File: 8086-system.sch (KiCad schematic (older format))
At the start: 0 parts

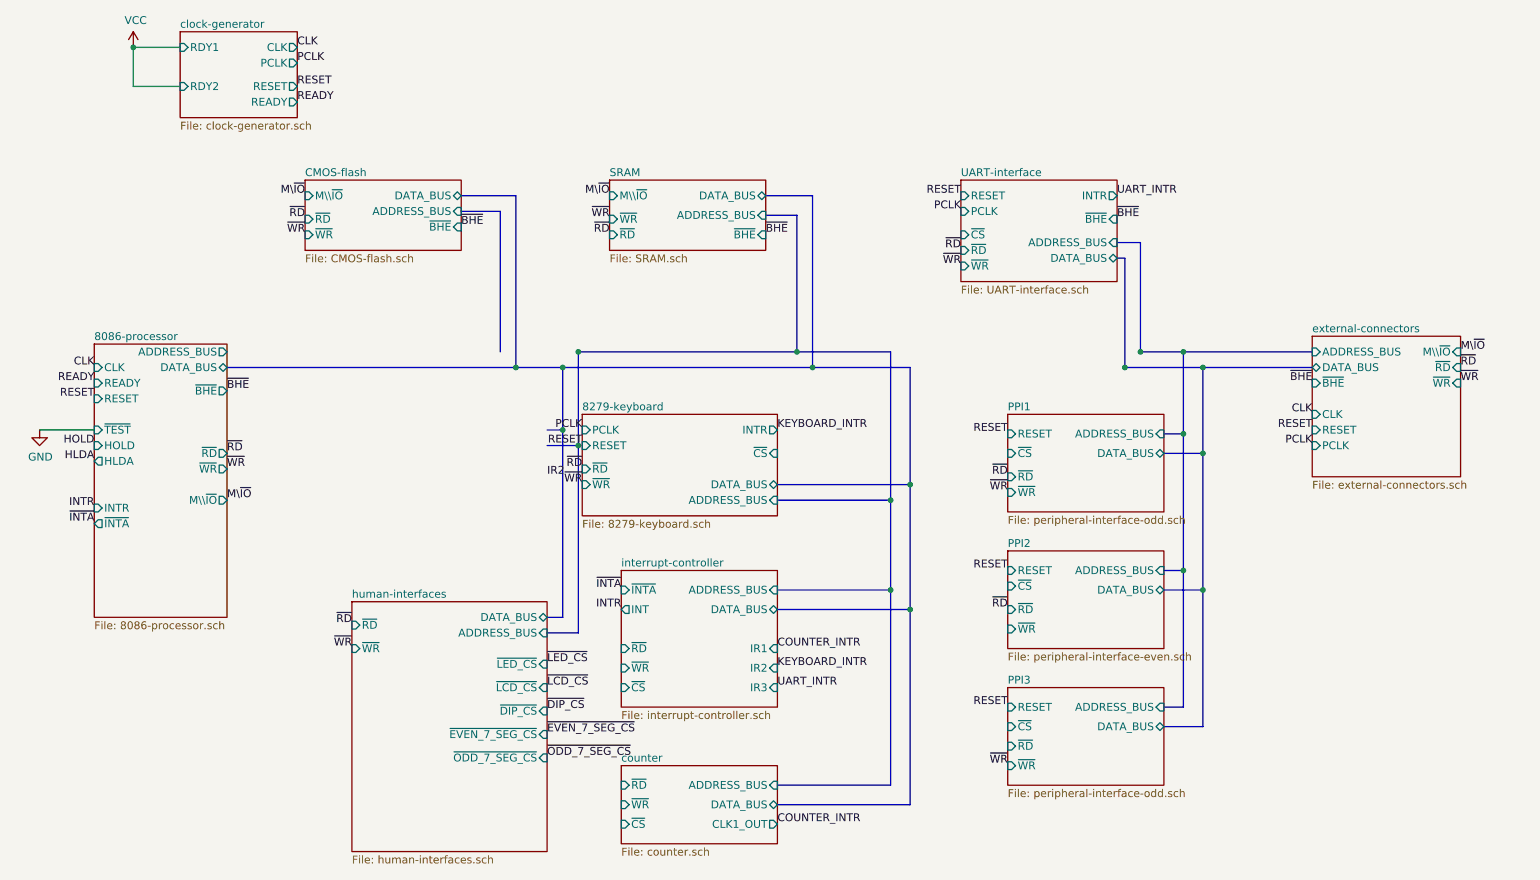
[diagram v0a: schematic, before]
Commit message: Fix wiring in root sheet
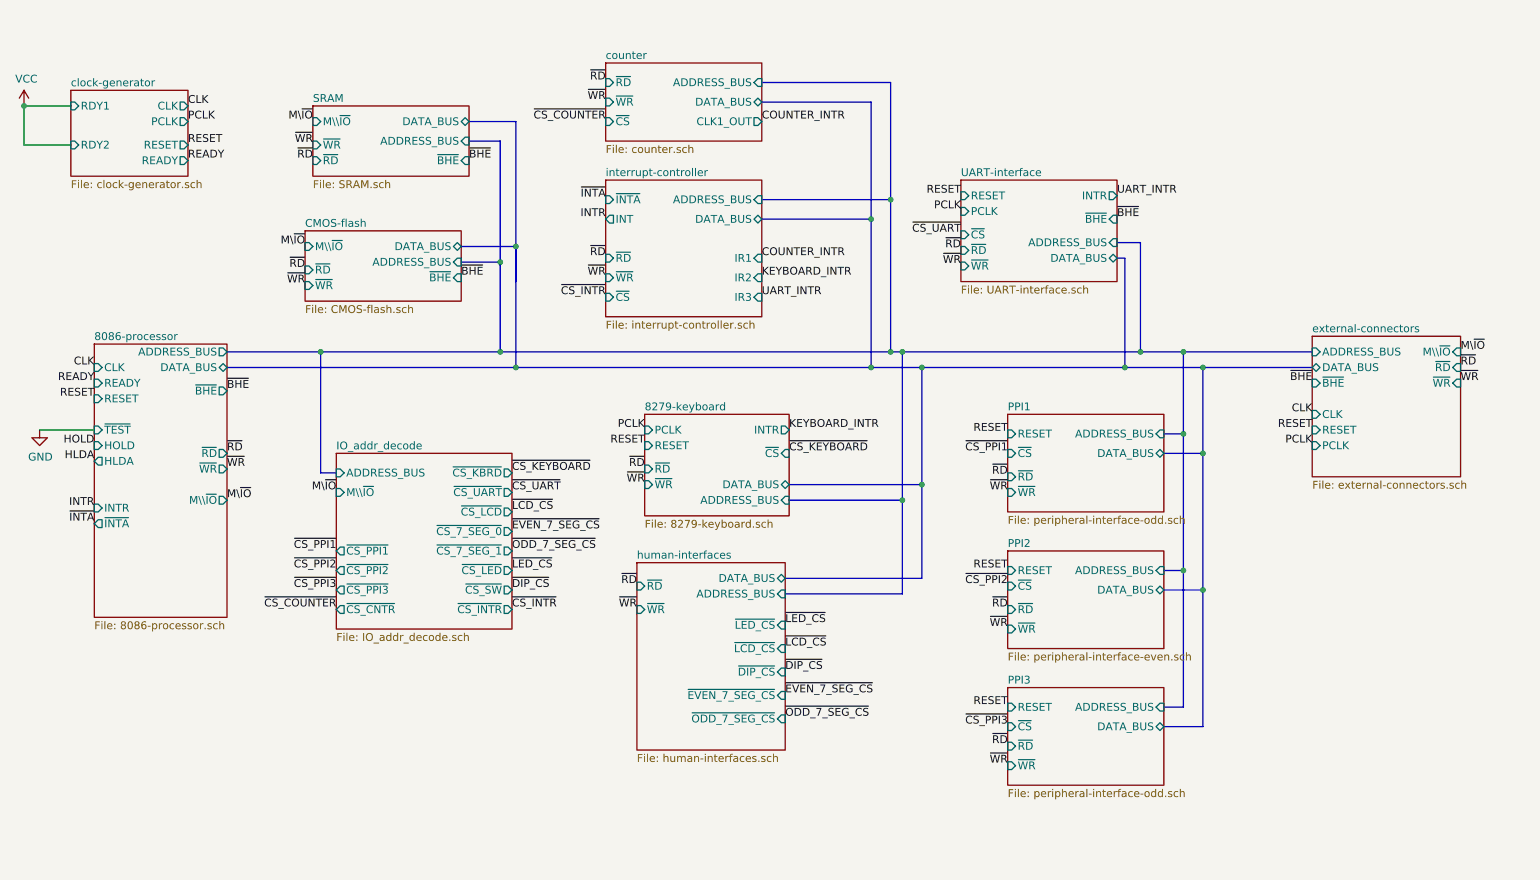
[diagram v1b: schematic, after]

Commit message: Decode BHE for IO addresses
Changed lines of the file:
@@
 F14 "~CS_7_SEG_0" O R 3825 4250 50
 F15 "~CS_7_SEG_1" O R 3825 4375 50
+F16 "~BHE" I L 2700 4125 50
 $EndSheet
 Connection ~ 6325 3100
@@
 Text Label 4675 3700 2    50   ~ 0
 RESET
+Text Label 2700 4125 2    50   ~ 0
+~BHE
 $EndSCHEMATC

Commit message: General edits; removed floating inputs
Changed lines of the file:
@@
 F4 "RESET" O R 1750 1775 50
 F5 "READY" O R 1750 1875 50
-F6 "RDY1" I L 1000 1525 50
-F7 "RDY2" I L 1000 1775 50
 $EndSheet
 Text Label 1750 1525 0    50   ~ 0
@@
 Text Label 1750 1775 0    50   ~ 0
 RESET
-Wire Wire Line
-	1150 3600 800  3600
-$Comp
-L power:GND #PWR0103
-U 1 1 61966AE7
-P 800 3600
-F 0 "#PWR0103" H 800 3350 50  0001 C CNN
-F 1 "GND" H 805 3427 50  0000 C CNN
-F 2 "" H 800 3600 50  0001 C CNN
-F 3 "" H 800 3600 50  0001 C CNN
-	1    800  3600
-	1    0    0    -1
-$EndComp
-Wire Wire Line
-	700  1525 700  1775
-$Comp
-L power:VCC #PWR0104
-U 1 1 61967609
-P 700 1525
-F 0 "#PWR0104" H 700 1375 50  0001 C CNN
-F 1 "VCC" H 715 1698 50  0000 C CNN
-F 2 "" H 700 1525 50  0001 C CNN
-F 3 "" H 700 1525 50  0001 C CNN
-	1    700  1525
-	1    0    0    -1
-$EndComp
-Wire Wire Line
-	1000 1775 700  1775
-Wire Wire Line
-	1000 1525 700  1525
-Connection ~ 700  1525
 Text Label 8950 3600 2    50   ~ 0
 RESET
@@
 F6 "RESET" I L 1150 3400 50
 F7 "READY" I L 1150 3300 50
-F8 "~TEST" I L 1150 3600 50
-F9 "HOLD" I L 1150 3700 50
-F10 "HLDA" O L 1150 3800 50
-F11 "~INTA" O L 1150 4200 50
-F12 "DATA_BUS" B R 2000 3200 50
-F13 "M\\~IO" O R 2000 4050 50
-F14 "~WR" O R 2000 3850 50
-F15 "~RD" O R 2000 3750 50
+F8 "HOLD" I L 1150 3700 50
+F9 "HLDA" O L 1150 3800 50
+F10 "~INTA" O L 1150 4200 50
+F11 "DATA_BUS" B R 2000 3200 50
+F12 "M\\~IO" O R 2000 4050 50
+F13 "~WR" O R 2000 3850 50
+F14 "~RD" O R 2000 3750 50
 $EndSheet
 Text Label 2000 3750 0    50   ~ 0

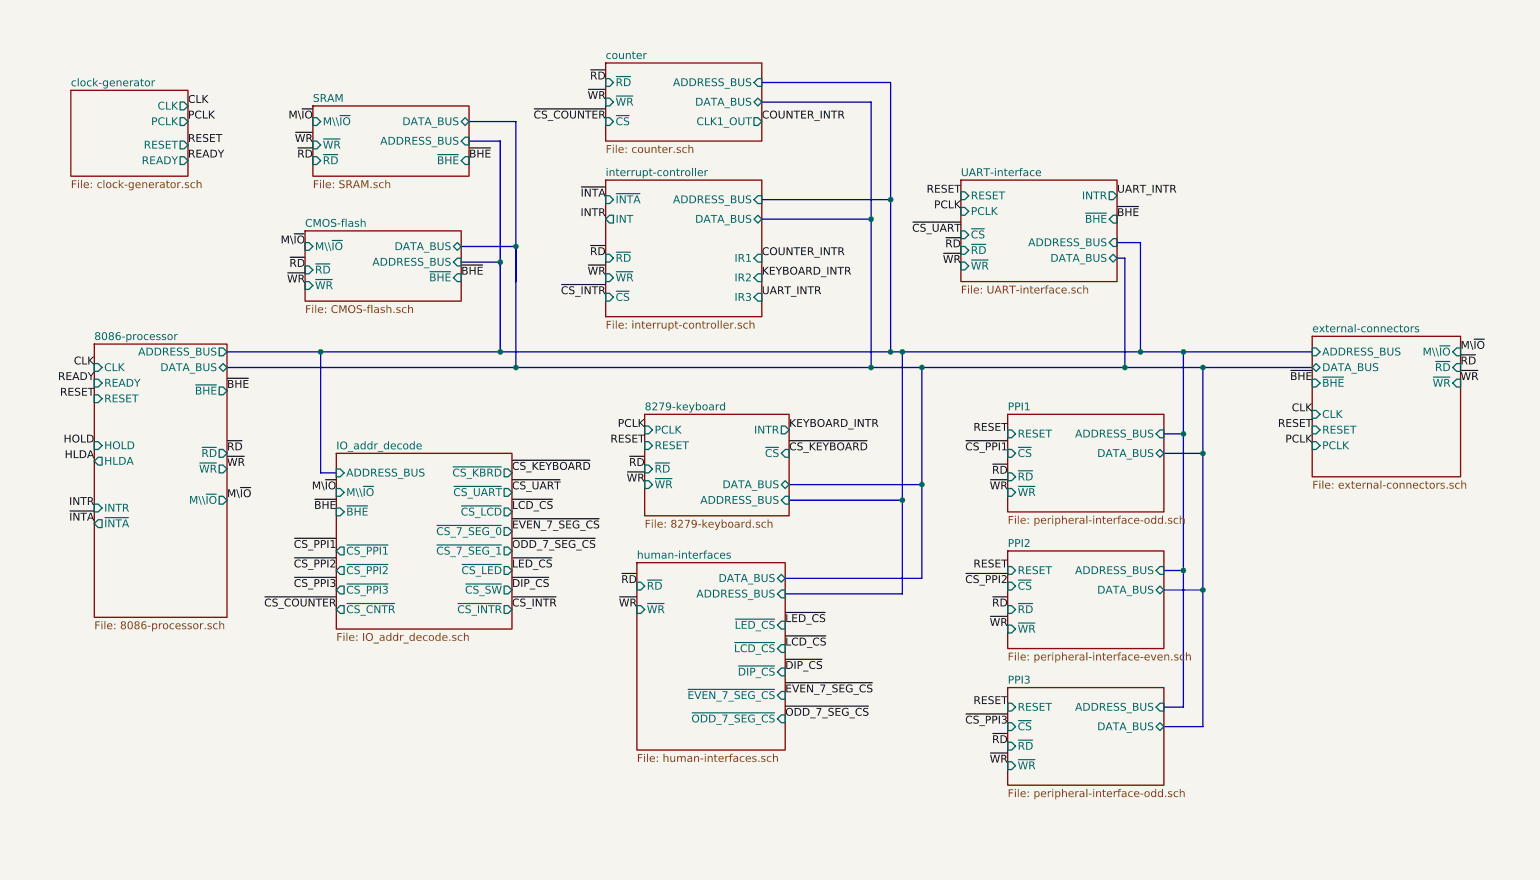
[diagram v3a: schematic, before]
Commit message: Updates to pass ERC
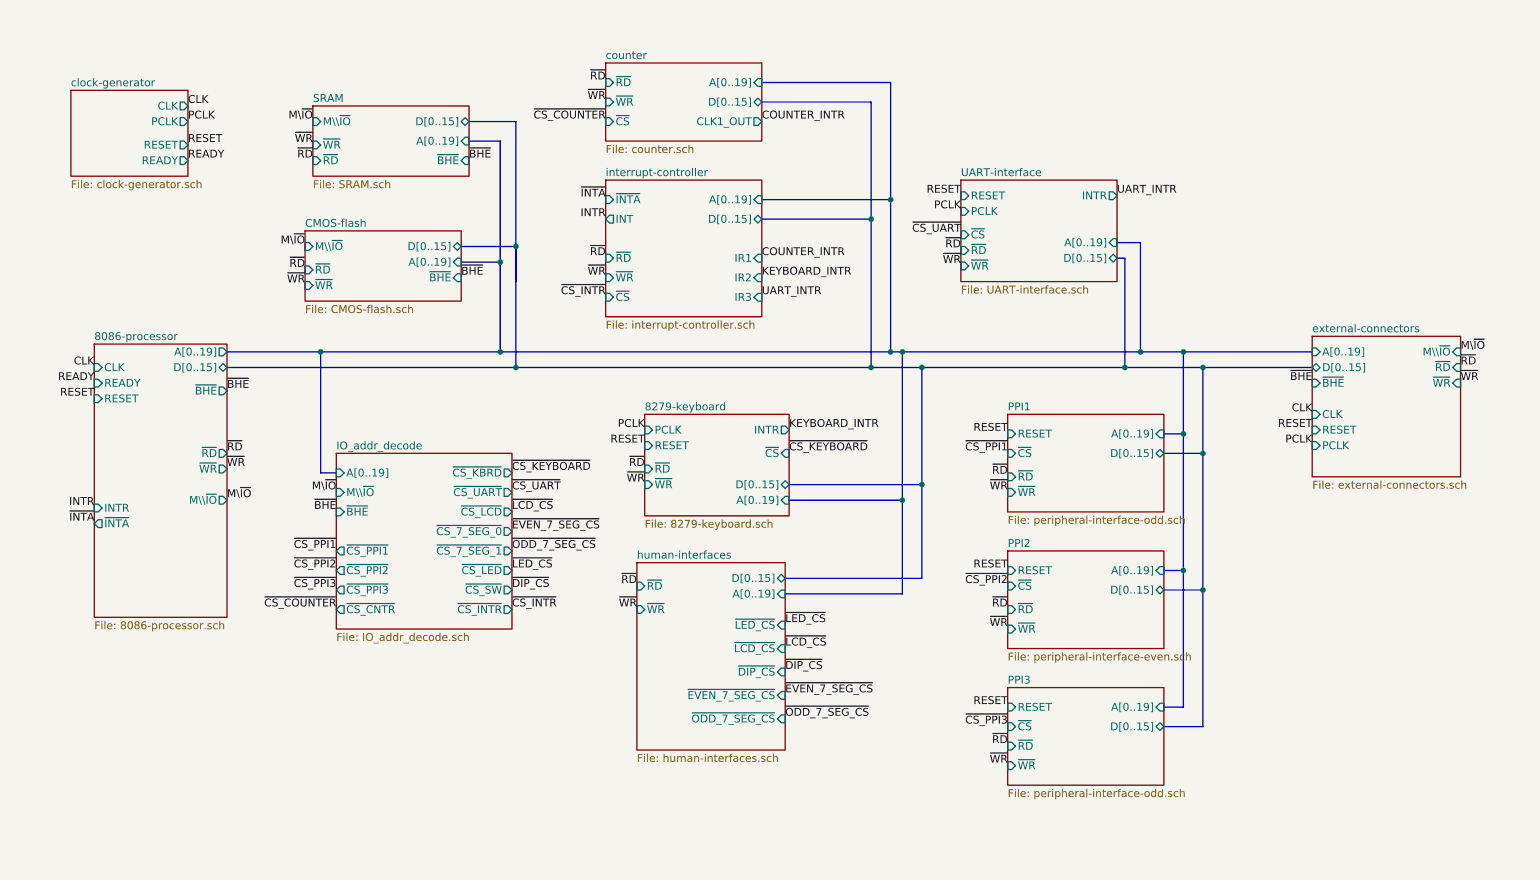
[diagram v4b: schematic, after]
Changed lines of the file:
@@
 F1 "external-connectors.sch" 50
 F2 "~BHE" I L 8950 3300 50
-F3 "DATA_BUS" B L 8950 3200 50
-F4 "ADDRESS_BUS" I L 8950 3100 50
+F3 "D[0..15]" B L 8950 3200 50
+F4 "A[0..19]" I L 8950 3100 50
 F5 "CLK" I L 8950 3500 50
 F6 "PCLK" I L 8950 3700 50
@@
 Text Label 1150 3400 2    50   ~ 0
 RESET
-Text Label 1150 3700 2    50   ~ 0
-HOLD
-Text Label 1150 3800 2    50   ~ 0
-HLDA
 Text Label 1150 4100 2    50   ~ 0
 INTR
@@
 F2 "INTR" O R 7700 2100 50
 F3 "PCLK" I L 6700 2200 50
-F4 "DATA_BUS" B R 7700 2500 50
+F4 "D[0..15]" B R 7700 2500 50
 F5 "RESET" I L 6700 2100 50
-F6 "ADDRESS_BUS" I R 7700 2400 50
-F7 "~BHE" I R 7700 2250 50
-F8 "~RD" I L 6700 2450 50
-F9 "~WR" I L 6700 2550 50
-F10 "~CS" I L 6700 2350 50
-$EndSheet
-Text Label 7700 2250 0    50   ~ 0
-~BHE
+F6 "A[0..19]" I R 7700 2400 50
+F7 "~RD" I L 6700 2450 50
+F8 "~WR" I L 6700 2550 50
+F9 "~CS" I L 6700 2350 50
+$EndSheet
 Text Label 7700 2100 0    50   ~ 0
 UART_INTR
@@
 F0 "SRAM" 50
 F1 "SRAM.sch" 50
-F2 "ADDRESS_BUS" I R 3550 1750 50
+F2 "A[0..19]" I R 3550 1750 50
 F3 "M\\~IO" I L 2550 1625 50
 F4 "~BHE" I R 3550 1875 50
 F5 "~RD" I L 2550 1875 50
 F6 "~WR" I L 2550 1775 50
-F7 "DATA_BUS" B R 3550 1625 50
+F7 "D[0..15]" B R 3550 1625 50
 $EndSheet
 Wire Bus Line
@@
 F4 "~RD" I L 7000 5625 50
 F5 "~WR" I L 7000 5750 50
-F6 "DATA_BUS" B R 8000 5500 50
-F7 "ADDRESS_BUS" I R 8000 5375 50
+F6 "D[0..15]" B R 8000 5500 50
+F7 "A[0..19]" I R 8000 5375 50
 $EndSheet
 $Sheet
@@
 F4 "~RD" I L 7000 3900 50
 F5 "~WR" I L 7000 4000 50
-F6 "DATA_BUS" B R 8000 3750 50
-F7 "ADDRESS_BUS" I R 8000 3625 50
+F6 "D[0..15]" B R 8000 3750 50
+F7 "A[0..19]" I R 8000 3625 50
 $EndSheet
 $Sheet
@@
 F4 "~RD" I L 7000 4750 50
 F5 "~WR" I L 7000 4875 50
-F6 "DATA_BUS" B R 8000 4625 50
-F7 "ADDRESS_BUS" I R 8000 4500 50
+F6 "D[0..15]" B R 8000 4625 50
+F7 "A[0..19]" I R 8000 4500 50
 $EndSheet
 $Sheet
@@
 F3 "IR2" I R 5425 2625 50
 F4 "IR3" I R 5425 2750 50
-F5 "DATA_BUS" B R 5425 2250 50
+F5 "D[0..15]" B R 5425 2250 50
 F6 "~CS" I L 4425 2750 50
 F7 "~WR" I L 4425 2625 50
@@
 F9 "INT" O L 4425 2250 50
 F10 "~INTA" I L 4425 2125 50
-F11 "ADDRESS_BUS" I R 5425 2125 50
+F11 "A[0..19]" I R 5425 2125 50
 $EndSheet
 Text Label 5600 3600 0    50   ~ 0
@@
 F3 "INTR" O R 5600 3600 50
 F4 "RESET" I L 4675 3700 50
-F5 "DATA_BUS" B R 5600 3950 50
-F6 "ADDRESS_BUS" I R 5600 4050 50
+F5 "D[0..15]" B R 5600 3950 50
+F6 "A[0..19]" I R 5600 4050 50
 F7 "~RD" I L 4675 3850 50
 F8 "~WR" I L 4675 3950 50
@@
 F0 "counter" 50
 F1 "counter.sch" 50
-F2 "DATA_BUS" B R 5425 1500 50
+F2 "D[0..15]" B R 5425 1500 50
 F3 "~RD" I L 4425 1375 50
 F4 "~WR" I L 4425 1500 50
-F5 "ADDRESS_BUS" I R 5425 1375 50
+F5 "A[0..19]" I R 5425 1375 50
 F6 "~CS" I L 4425 1625 50
 F7 "CLK1_OUT" O R 5425 1625 50
@@
 F1 "8086-processor.sch" 50
 F2 "CLK" I L 1150 3200 50
-F3 "ADDRESS_BUS" O R 2000 3100 50
+F3 "A[0..19]" O R 2000 3100 50
 F4 "~BHE" O R 2000 3350 50
 F5 "INTR" I L 1150 4100 50
 F6 "RESET" I L 1150 3400 50
 F7 "READY" I L 1150 3300 50
-F8 "HOLD" I L 1150 3700 50
-F9 "HLDA" O L 1150 3800 50
-F10 "~INTA" O L 1150 4200 50
-F11 "DATA_BUS" B R 2000 3200 50
-F12 "M\\~IO" O R 2000 4050 50
-F13 "~WR" O R 2000 3850 50
-F14 "~RD" O R 2000 3750 50
+F8 "~INTA" O L 1150 4200 50
+F9 "D[0..15]" B R 2000 3200 50
+F10 "M\\~IO" O R 2000 4050 50
+F11 "~WR" O R 2000 3850 50
+F12 "~RD" O R 2000 3750 50
 $EndSheet
 Text Label 2000 3750 0    50   ~ 0
@@
 F0 "CMOS-flash" 50
 F1 "CMOS-flash.sch" 50
-F2 "DATA_BUS" B R 3500 2425 50
-F3 "ADDRESS_BUS" I R 3500 2525 50
+F2 "D[0..15]" B R 3500 2425 50
+F3 "A[0..19]" I R 3500 2525 50
 F4 "M\\~IO" I L 2500 2425 50
 F5 "~BHE" I R 3500 2625 50
@@
 F0 "IO_addr_decode" 50
 F1 "IO_addr_decode.sch" 50
-F2 "ADDRESS_BUS" I L 2700 3875 50
+F2 "A[0..19]" I L 2700 3875 50
 F3 "M\\~IO" I L 2700 4000 50
 F4 "~CS_PPI1" O L 2700 4375 50
@@
 F0 "human-interfaces" 50
 F1 "human-interfaces.sch" 50
-F2 "DATA_BUS" B R 5575 4550 50
-F3 "ADDRESS_BUS" I R 5575 4650 50
+F2 "D[0..15]" B R 5575 4550 50
+F3 "A[0..19]" I R 5575 4650 50
 F4 "~LED_CS" I R 5575 4850 50
 F5 "~LCD_CS" I R 5575 5000 50
